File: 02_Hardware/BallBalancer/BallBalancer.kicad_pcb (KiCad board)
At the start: 2 copper layers, 43 parts, among them J1 ENCODER1_CON, J2 ENCODER2_CON, J3 USB_B_Micro, J4 SWD, Q1 DMN10H220L, U1 STM32L412K8Tx, U2 USBLC6-2SC6, U3 AP63203WU

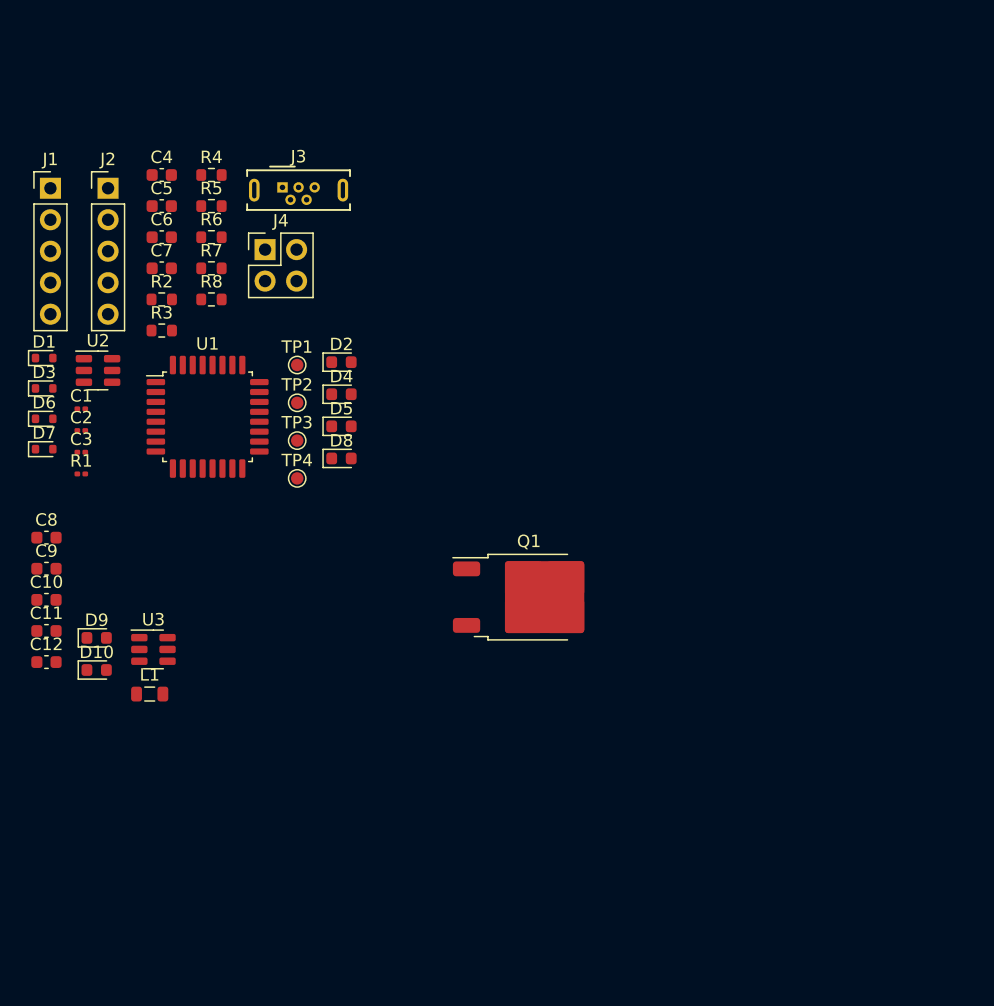
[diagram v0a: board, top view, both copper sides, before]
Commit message: Hardware schema and layout created
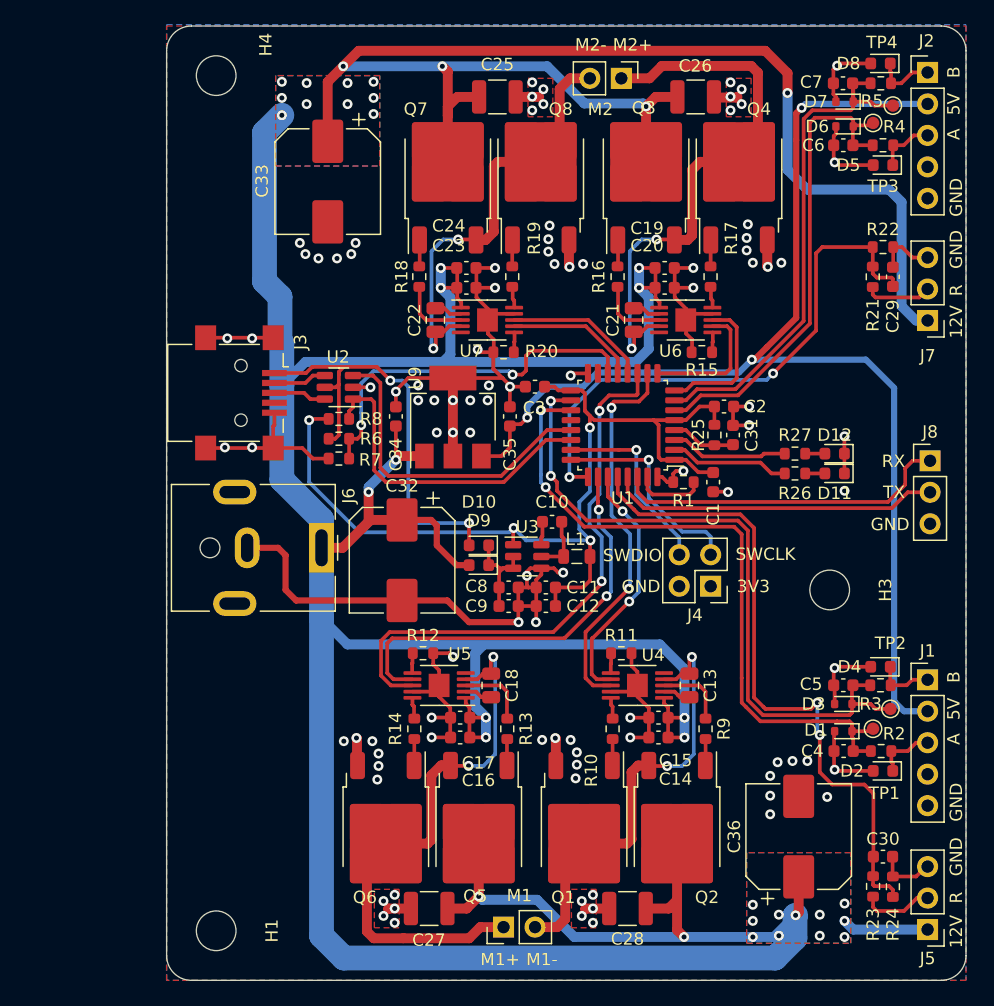
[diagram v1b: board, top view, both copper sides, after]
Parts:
- added C13: 1u, Capacitor_SMD:C_0805_2012Metric, F.Cu at (124.7, 111.2)
- added C14: 1u, Capacitor_SMD:C_0603_1608Metric, F.Cu at (122.2, 115.4)
- added C15: 100n, Capacitor_SMD:C_0603_1608Metric, F.Cu at (122.2, 113.8)
- added C16: 1u, Capacitor_SMD:C_0603_1608Metric, F.Cu at (106.2, 115.4)
- added C17: 100n, Capacitor_SMD:C_0603_1608Metric, F.Cu at (106.2, 113.8)
- added C18: 1u, Capacitor_SMD:C_0805_2012Metric, F.Cu at (108.7, 111.2)
- added C19: 1u, Capacitor_SMD:C_0603_1608Metric, F.Cu at (122.7, 77.5)
- added C20: 100n, Capacitor_SMD:C_0603_1608Metric, F.Cu at (122.7, 79.1)
- added C21: 1u, Capacitor_SMD:C_0805_2012Metric, F.Cu at (120.2, 81.7)
- added C22: 1u, Capacitor_SMD:C_0805_2012Metric, F.Cu at (104.2, 81.7)
- added C23: 100n, Capacitor_SMD:C_0603_1608Metric, F.Cu at (106.7, 79.1)
- added C24: 1u, Capacitor_SMD:C_0603_1608Metric, F.Cu at (106.7, 77.5)
- added C25: 10U, Capacitor_SMD:C_1210_3225Metric, F.Cu at (109.2, 63.7)
- added C26: 10U, Capacitor_SMD:C_1210_3225Metric, F.Cu at (125.2, 63.7)
- added C27: 10U, Capacitor_SMD:C_1210_3225Metric, F.Cu at (103.7, 129.2)
- added C28: 10U, Capacitor_SMD:C_1210_3225Metric, F.Cu at (119.7, 129.2)
- added C29: 100n, Capacitor_SMD:C_0603_1608Metric, F.Cu at (141.1, 78.2)
- added C30: 100n, Capacitor_SMD:C_0603_1608Metric, F.Cu at (140.3, 125.0)
- added C31: 100n, Capacitor_SMD:C_0603_1608Metric, F.Cu at (128.2, 91.0)
- added C32: 330u, Capacitor_SMD:CP_Elec_8x10, F.Cu at (101.5, 101.1)
- added C33: 330u, Capacitor_SMD:CP_Elec_8x10, F.Cu at (95.5, 70.5)
- added C34: 100n, Capacitor_SMD:C_0603_1608Metric, F.Cu at (101.0, 89.5)
- added C35: 100n, Capacitor_SMD:C_0603_1608Metric, F.Cu at (110.2, 89.5)
- added C36: 330u, Capacitor_SMD:CP_Elec_8x10, F.Cu at (133.5, 123.4)
- added D11: LED, LED_SMD:LED_0603_1608Metric, F.Cu at (136.4, 94.1)
- added D12: LED, LED_SMD:LED_0603_1608Metric, F.Cu at (136.4, 92.5)
- added H1: MountingHole, MountingHole:MountingHole_3.2mm_M3, F.Cu at (86.5, 131.0)
- added H3: MountingHole, MountingHole:MountingHole_3.2mm_M3, F.Cu at (136.0, 103.5)
- added H4: MountingHole, MountingHole:MountingHole_3.2mm_M3, F.Cu at (86.5, 62.0)
- added J5: Conn_01x03_Pin, Connector_PinHeader_2.54mm:PinHeader_1x03_P2.54mm_Vertical, F.Cu at (143.9, 130.9)
- added J6: Jack-DC, Connector_BarrelJack:BarrelJack_CUI_PJ-063AH_Horizontal, F.Cu at (95.0, 100.1)
- added J7: Conn_01x03_Pin, Connector_PinHeader_2.54mm:PinHeader_1x03_P2.54mm_Vertical, F.Cu at (143.9, 81.8)
- added J8: Conn_01x03_Pin, Connector_PinHeader_2.54mm:PinHeader_1x03_P2.54mm_Vertical, F.Cu at (144.1, 93.1)
- added M1: Motor_DC, Connector_PinHeader_2.54mm:PinHeader_1x02_P2.54mm_Vertical, F.Cu at (109.7, 130.7)
- added M2: Motor_DC, Connector_PinHeader_2.54mm:PinHeader_1x02_P2.54mm_Vertical, F.Cu at (119.2, 62.2)
- added Q2: DMN10H220L, Package_TO_SOT_SMD:TO-252-2, F.Cu at (123.7, 122.7)
- added Q3: DMN10H220L, Package_TO_SOT_SMD:TO-252-2, F.Cu at (121.2, 70.2)
- added Q4: DMN10H220L, Package_TO_SOT_SMD:TO-252-2, F.Cu at (128.7, 70.2)
- added Q5: DMN10H220L, Package_TO_SOT_SMD:TO-252-2, F.Cu at (107.7, 122.7)
- added Q6: DMN10H220L, Package_TO_SOT_SMD:TO-252-2, F.Cu at (100.2, 122.7)
- added Q7: DMN10H220L, Package_TO_SOT_SMD:TO-252-2, F.Cu at (105.2, 70.2)
- added Q8: DMN10H220L, Package_TO_SOT_SMD:TO-252-2, F.Cu at (112.7, 70.2)
- added R10: 20, Resistor_SMD:R_0603_1608Metric, F.Cu at (118.5, 114.7)
- added R11: 10k, Resistor_SMD:R_0603_1608Metric, F.Cu at (119.2, 108.6)
- added R12: 10k, Resistor_SMD:R_0603_1608Metric, F.Cu at (103.2, 108.6)
- added R13: 20, Resistor_SMD:R_0603_1608Metric, F.Cu at (110.0, 114.7)
- added R14: 20, Resistor_SMD:R_0603_1608Metric, F.Cu at (102.5, 114.7)
- added R15: 10k, Resistor_SMD:R_0603_1608Metric, F.Cu at (125.7, 84.3)
- added R16: 20, Resistor_SMD:R_0603_1608Metric, F.Cu at (118.9, 78.2)
- added R17: 20, Resistor_SMD:R_0603_1608Metric, F.Cu at (126.4, 78.2)
- added R18: 20, Resistor_SMD:R_0603_1608Metric, F.Cu at (102.9, 78.2)
- added R19: 20, Resistor_SMD:R_0603_1608Metric, F.Cu at (110.4, 78.2)
- added R20: 10k, Resistor_SMD:R_0603_1608Metric, F.Cu at (109.7, 84.3)
- added R21: 10k, Resistor_SMD:R_0603_1608Metric, F.Cu at (139.5, 78.2)
- added R22: 10k, Resistor_SMD:R_0603_1608Metric, F.Cu at (140.3, 75.8)
- added R23: 10k, Resistor_SMD:R_0603_1608Metric, F.Cu at (139.5, 127.4)
- added R24: 10k, Resistor_SMD:R_0603_1608Metric, F.Cu at (141.1, 127.4)
- added R25: 100K, Resistor_SMD:R_0603_1608Metric, F.Cu at (126.7, 91.0)
- added R26: 240, Resistor_SMD:R_0603_1608Metric, F.Cu at (133.2, 94.1)
- added R27: 240, Resistor_SMD:R_0603_1608Metric, F.Cu at (133.2, 92.5)
- added R9: 20, Resistor_SMD:R_0603_1608Metric, F.Cu at (126.0, 114.7)
- added U4: DGD0506A, Package_SO:MSOP-10-1EP_3x3mm_P0.5mm_EP1.68x1.88mm, F.Cu at (120.5, 111.2)
- added U5: DGD0506A, Package_SO:MSOP-10-1EP_3x3mm_P0.5mm_EP1.68x1.88mm, F.Cu at (104.5, 111.2)
- added U6: DGD0506A, Package_SO:MSOP-10-1EP_3x3mm_P0.5mm_EP1.68x1.88mm, F.Cu at (124.4, 81.7)
- added U7: DGD0506A, Package_SO:MSOP-10-1EP_3x3mm_P0.5mm_EP1.68x1.88mm, F.Cu at (108.4, 81.7)
- added U9: LM2937IMP5, Package_TO_SOT_SMD:SOT-223-3_TabPin2, F.Cu at (105.6, 89.5)
- C1, C2, C3: footprint Capacitor_SMD:C_0201_0603Metric -> Capacitor_SMD:C_0603_1608Metric
- J3: footprint Connector_USB:USB_Micro-B_Wuerth_614105150721_Vertical -> Connector_USB:USB_Mini-B_Lumberg_2486_01_Horizontal
- R1: footprint Resistor_SMD:R_0201_0603Metric -> Resistor_SMD:R_0603_1608Metric
- moved J1 81.1 mm to (143.9, 110.7)
- moved C4 72.0 mm to (137.1, 116.5), turned to 180 degrees
- moved D1 71.2 mm to (137.1, 114.9), turned to 180 degrees
- moved D7 70.4 mm to (137.2, 64.1), turned to 180 degrees
- moved D3 69.3 mm to (137.1, 112.7), turned to 180 degrees
- moved D6 68.8 mm to (137.2, 66.1), turned to 180 degrees
- moved R2 68.5 mm to (140.2, 116.5), turned to 180 degrees
- moved C5 67.2 mm to (137.1, 111.2), turned to 180 degrees
- moved J2 66.8 mm to (143.9, 61.7)
- moved R3 64.7 mm to (140.1, 111.2), turned to 180 degrees
- moved C7 57.0 mm to (137.1, 62.6), turned to 180 degrees
- moved TP4 56.7 mm to (141.1, 64.4)
- moved C6 55.5 mm to (137.1, 67.6), turned to 180 degrees
- moved TP1 55.0 mm to (139.5, 114.7)
- moved R5 54.9 mm to (140.1, 62.6), turned to 180 degrees
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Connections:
- net ENCODER1_A_OUT renamed /Main/ENCODER1_A_OUT
- net ENCODER1_B_OUT renamed /Main/ENCODER1_B_OUT
- net ENCODER2_A_OUT renamed /Main/ENCODER2_A_OUT
- net ENCODER2_B_OUT renamed /Main/ENCODER2_B_OUT
- C4 pad 1: ENCODER1_A -> /Main/ENCODER1_A
- C5 pad 1: ENCODER1_B -> /Main/ENCODER1_B
- C6 pad 1: ENCODER2_A -> /Main/ENCODER2_A
- C7 pad 1: ENCODER2_B -> /Main/ENCODER2_B
- D1 pad 1: ENCODER1_A -> /Main/ENCODER1_A
- D3 pad 1: ENCODER1_B -> /Main/ENCODER1_B
- D6 pad 1: ENCODER2_A -> /Main/ENCODER2_A
- D7 pad 1: ENCODER2_B -> /Main/ENCODER2_B
- J1 pad 4: ENCODER1_INDEX -> unconnected-(J1-Pin_4-Pad4)
- J2 pad 4: ENCODER2_INDEX -> unconnected-(J2-Pin_4-Pad4)
- J4 pad 3: SWCLK -> /Main/SWCLK
- J4 pad 4: SWDIO -> /Main/SWDIO
- Q1 pad 1: unconnected-(Q1-G-Pad1) -> Net-(Q1-G)
- Q1 pad 2: unconnected-(Q1-S-Pad2) -> Net-(M1--)
- Q1 pad 3: unconnected-(Q1-D-Pad3) -> GND
- R1 pad 1: Net-(U1-PB7) -> GND
- R1 pad 2: GND -> Net-(U1-PH3)
- R2 pad 2: ENCODER1_A -> /Main/ENCODER1_A
- R3 pad 2: ENCODER1_B -> /Main/ENCODER1_B
- R4 pad 2: ENCODER2_A -> /Main/ENCODER2_A
- R5 pad 2: ENCODER2_B -> /Main/ENCODER2_B
- R6 pad 2: VUSB -> /Main/VUSB
- R7 pad 2: VUSB -> /Main/VUSB
- R8 pad 1: USB_DP -> /Main/USB_DP
- TP1 pad 1: ENCODER1_A -> /Main/ENCODER1_A
- TP2 pad 1: ENCODER1_B -> /Main/ENCODER1_B
- TP3 pad 1: ENCODER2_A -> /Main/ENCODER2_A
- TP4 pad 1: ENCODER2_B -> /Main/ENCODER2_B
- U1 pad 10: unconnected-(U1-PA4-Pad10) -> IN_MOT_CH1L
- U1 pad 11: unconnected-(U1-PA5-Pad11) -> IN_MOT_CH1R
- U1 pad 12: unconnected-(U1-PA6-Pad12) -> IN_MOT_CH2L
- U1 pad 13: unconnected-(U1-PA7-Pad13) -> EN_MOT_CH2L
- U1 pad 14: unconnected-(U1-PB0-Pad14) -> /Main/VUSB
- U1 pad 18: unconnected-(U1-PA8-Pad18) -> /Main/ENCODER1_B
- U1 pad 19: unconnected-(U1-PA9-Pad19) -> /Main/ENCODER1_A
- U1 pad 2: unconnected-(U1-PC14-Pad2) -> /Main/LED1
- U1 pad 21: unconnected-(U1-PA11-Pad21) -> /Main/USB_DM
- U1 pad 22: unconnected-(U1-PA12-Pad22) -> /Main/USB_DP
- U1 pad 23: unconnected-(U1-PA13-Pad23) -> /Main/SWDIO
- U1 pad 24: unconnected-(U1-PA14-Pad24) -> /Main/SWCLK
- U1 pad 25: unconnected-(U1-PA15-Pad25) -> /Main/REF_MOT2
- U1 pad 26: unconnected-(U1-PB3-Pad26) -> EN_MOT_CH1R
- U1 pad 27: unconnected-(U1-PB4-Pad27) -> EN_MOT_CH1L
- U1 pad 28: unconnected-(U1-PB5-Pad28) -> /Main/REF_MOT1
- U1 pad 29: unconnected-(U1-PB6-Pad29) -> /Main/RSPI_TX
- U1 pad 3: unconnected-(U1-PC15-Pad3) -> /Main/LED2
- U1 pad 30: Net-(U1-PB7) -> /Main/RSPI_RX
- U1 pad 31: unconnected-(U1-PH3-Pad31) -> Net-(U1-PH3)
- U1 pad 4: unconnected-(U1-NRST-Pad4) -> Net-(U1-NRST)
- U1 pad 6: unconnected-(U1-PA0-Pad6) -> /Main/ENCODER2_A
- U1 pad 7: unconnected-(U1-PA1-Pad7) -> /Main/ENCODER2_B
- U1 pad 8: unconnected-(U1-PA2-Pad8) -> IN_MOT_CH2R
- U1 pad 9: unconnected-(U1-PA3-Pad9) -> EN_MOT_CH2R
- U2 pad 1: USB_DP -> /Main/USB_DP
- U2 pad 3: USB_DM -> /Main/USB_DM
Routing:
- net +12V: track 0.00 -> 424.7 mm, vias 0 -> 37
- net GND: track 0.00 -> 201.2 mm, vias 0 -> 99
- net +5V: track 0.00 -> 99.7 mm, vias 0 -> 3
- net +3V3: track 0.00 -> 77.7 mm, vias 0 -> 4
- net /Main/ENCODER1_B: track 0.00 -> 55.4 mm, vias 0 -> 2
- net /Main/ENCODER1_A: track 0.00 -> 54.9 mm, vias 0 -> 2
- net /Main/REF_MOT1: track 0.00 -> 53.3 mm, vias 0 -> 2
- net IN_MOT_CH1R: track 0.00 -> 45.7 mm, vias 0 -> 2
- net /Main/REF_MOT2: track 0.00 -> 45.0 mm, vias 0 -> 2
- net Net-(M2-+): track 0.00 -> 43.7 mm, vias 0 -> 2
- net Net-(M1-+): track 0.00 -> 43.5 mm, vias 0 -> 2
- net /Main/ENCODER2_B: track 0.00 -> 42.1 mm
- net /Main/ENCODER2_A: track 0.00 -> 39.2 mm
- net VBUS: track 0.00 -> 36.8 mm, vias 0 -> 2
- net EN_MOT_CH1R: track 0.00 -> 34.1 mm, vias 0 -> 2
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- added copper zone on B.Cu, net +12V
- added copper zone on F.Cu, net +12V
- added copper zone on B.Cu, net GND
- added copper zone on F.Cu, net GND
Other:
- board outline added: 64.5 x 77 mm
- board text added: "12V"
- board text added: "3V3"
- board text added: "5V"
- board text added: "A"
- board text added: "B"
- board text added: "GND"
- board text added: "M1+"
- board text added: "M1-"
- board text added: "M2+"
- board text added: "M2-"
- board text added: "R"
- board text added: "RX"
- board text added: "SWCLK"
- board text added: "SWDIO"
- board text added: "TX"

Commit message: ERC and DRC warnings and errors in schema and layout fixed
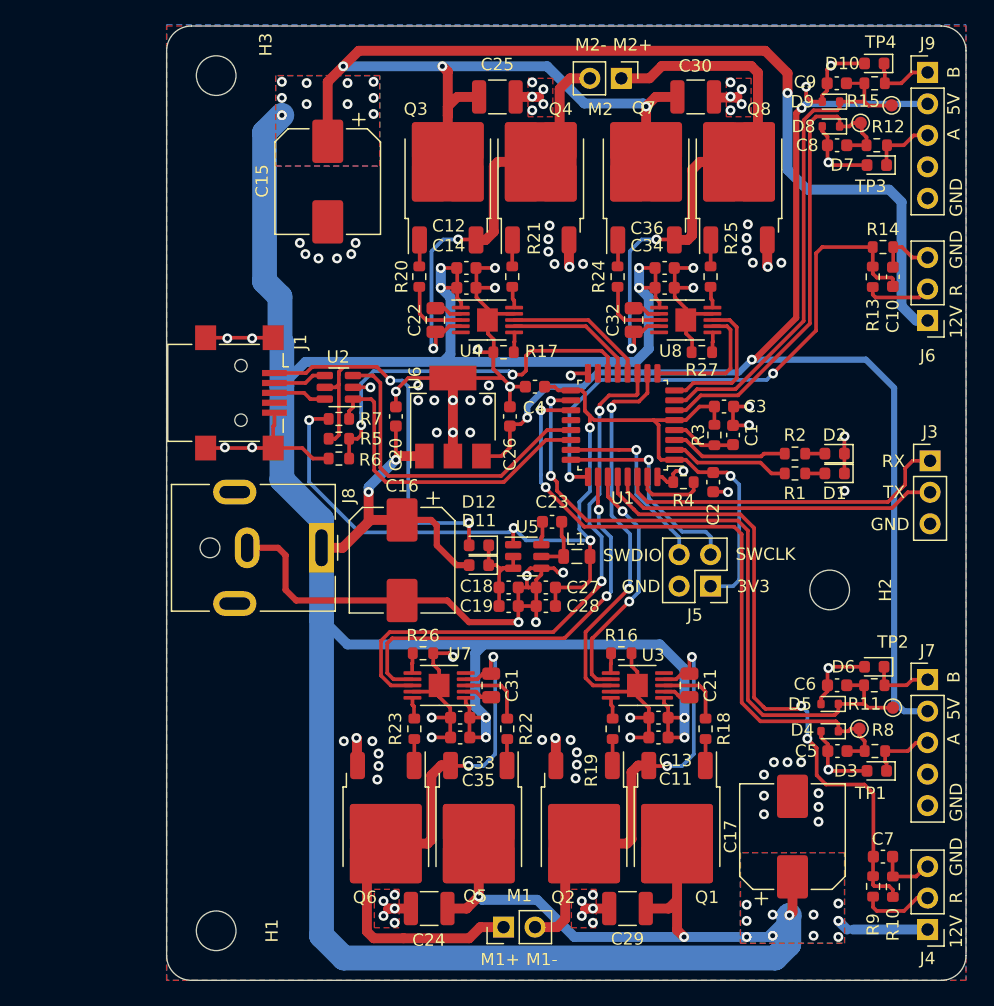
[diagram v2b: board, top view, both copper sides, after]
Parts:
- removed the J1 at (143.9, 110.7)
- removed J2: ENCODER2_CON, Connector_PinHeader_2.54mm:PinHeader_1x05_P2.54mm_Vertical
- removed the J4 at (126.4, 103.2)
- added J5: SWD, Connector_PinHeader_2.54mm:PinHeader_2x02_P2.54mm_Vertical, F.Cu at (126.4, 103.2)
- added J7: ENCODER 1, Connector_PinHeader_2.54mm:PinHeader_1x05_P2.54mm_Vertical, F.Cu at (143.9, 110.7)
- added J9: ENCODER 2, Connector_PinHeader_2.54mm:PinHeader_1x05_P2.54mm_Vertical, F.Cu at (143.9, 61.7)
- J3: renamed from J8; value Conn_01x03_Pin -> Raspberry PI UART
- J4: renamed from J5; value Conn_01x03_Pin -> Reference switch 1
- J6: renamed from J7; value Conn_01x03_Pin -> Reference switch 2
- R10: renamed from R24; value 10k -> 1K
- R13: renamed from R21; value 10k -> 2.7K
- R14: renamed from R22; value 10k -> 1K
- R9: renamed from R23; value 10k -> 2.7K
- moved D4 1.10 mm to (136.0, 114.9)
- moved D5 1.10 mm to (136.0, 112.7)
- moved D8 1.10 mm to (136.1, 66.1)
- moved D9 1.10 mm to (136.1, 64.1)
- moved TP1 1.10 mm to (138.4, 114.7)
- moved TP3 1.00 mm to (138.5, 65.8)
- moved C17 0.50 mm to (133.0, 123.4)
- moved C5 0.50 mm to (136.6, 116.5)
- moved C6 0.50 mm to (136.6, 111.2)
- moved C8 0.50 mm to (136.6, 67.6)
- moved C9 0.50 mm to (136.6, 62.6)
- moved D10 0.50 mm to (139.6, 61.0)
- moved D3 0.50 mm to (139.8, 118.1)
- moved D6 0.50 mm to (139.6, 109.7)
- moved D7 0.50 mm to (139.8, 69.2)
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- renumbered C31 to C1, C29 to C10, C14 to C11, C24 to C12, C15 to C13, C23 to C14, C33 to C15, C32 to C16, C36 to C17, C8 to C18, C9 to C19, C1 to C2, C34 to C20, C13 to C21, C10 to C23, C27 to C24, C35 to C26, C11 to C27, C12 to C28, C28 to C29, C2 to C3, C26 to C30, C18 to C31, C21 to C32, C17 to C33, C20 to C34, C16 to C35, C19 to C36, C3 to C4, C4 to C5, C5 to C6, C30 to C7, C6 to C8, C7 to C9, D11 to D1, D8 to D10, D9 to D11, D10 to D12, D12 to D2, D2 to D3, D1 to D4, D3 to D5, D4 to D6, D5 to D7, D6 to D8, D7 to D9, H3 to H2, H4 to H3, J3 to J1, J6 to J8, Q2 to Q1, Q1 to Q2, Q7 to Q3, Q8 to Q4, Q3 to Q7, Q4 to Q8, R26 to R1, R3 to R11, R4 to R12, R5 to R15, R11 to R16, R20 to R17, R9 to R18, R10 to R19, R27 to R2, R18 to R20, R19 to R21, R13 to R22, R14 to R23, R16 to R24, R17 to R25, R12 to R26, R15 to R27, R25 to R3, R1 to R4, R6 to R5, R7 to R6, R8 to R7, R2 to R8, U4 to U3, U7 to U4, U3 to U5, U9 to U6, U5 to U7, U6 to U8
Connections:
- net Net-(D10-K) renamed +12VA
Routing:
- net +3V3: track 77.7 -> 90.4 mm, vias 4 -> 5
- net GND: track 201.2 -> 203.8 mm, vias 99 -> 102
- net /Main/ENCODER2_B: track 42.1 -> 40.0 mm
- net /Main/REF_MOT1: track 53.3 -> 52.5 mm
- net /Main/ENCODER1_A: track 54.9 -> 54.1 mm
- net /Main/ENCODER2_B_OUT: track 4.94 -> 5.44 mm
- net /Main/ENCODER2_A_OUT: track 4.72 -> 5.22 mm
- net /Main/ENCODER1_B_OUT: track 4.66 -> 5.16 mm
- net /Main/ENCODER1_A_OUT: track 4.85 -> 5.35 mm

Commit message: Test points added and BOM created
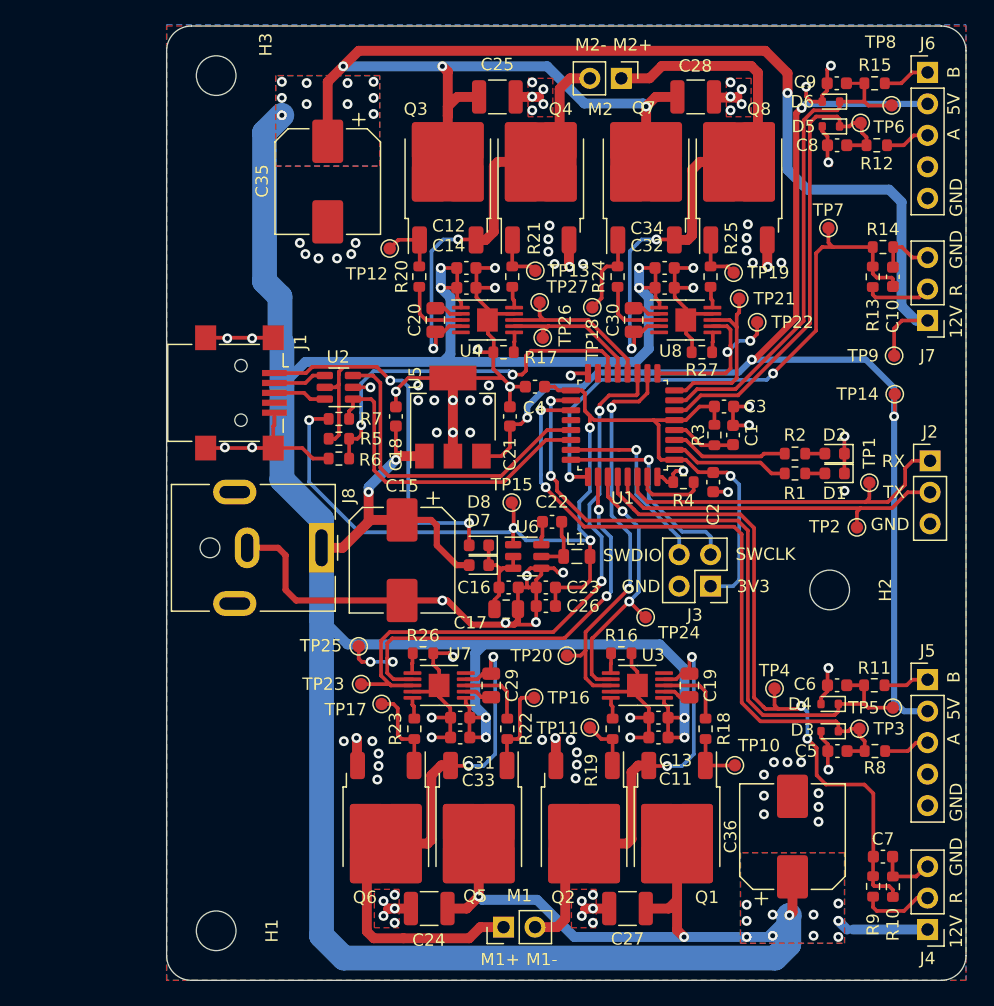
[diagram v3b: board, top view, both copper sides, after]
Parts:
- removed D10: D_TVS, Diode_SMD:D_0603_1608Metric
- removed the D3 at (139.8, 118.1)
- removed the D6 at (139.6, 109.7)
- removed the D7 at (139.8, 69.2)
- added TP1: UART_RX, TestPoint:TestPoint_Pad_D1.0mm, F.Cu at (139.2, 94.8)
- added TP10: GH_CH1L, TestPoint:TestPoint_Pad_D1.0mm, F.Cu at (128.3, 117.7)
- added TP11: GL_CH1L, TestPoint:TestPoint_Pad_D1.0mm, F.Cu at (116.7, 114.6)
- added TP12: GH_CH2L, TestPoint:TestPoint_Pad_D1.0mm, F.Cu at (100.5, 76.0)
- added TP13: GL_CH2L, TestPoint:TestPoint_Pad_D1.0mm, F.Cu at (112.2, 77.8)
- added TP14: 5V, TestPoint:TestPoint_Pad_D1.0mm, F.Cu at (141.2, 87.7)
- added TP15: 3.3V, TestPoint:TestPoint_Pad_D1.0mm, F.Cu at (110.3, 96.5)
- added TP16: GH_CH1R, TestPoint:TestPoint_Pad_D1.0mm, F.Cu at (112.2, 112.2)
- added TP17: GL_CH1R, TestPoint:TestPoint_Pad_D1.0mm, F.Cu at (99.8, 112.7)
- added TP18: GH_CH2R, TestPoint:TestPoint_Pad_D1.0mm, F.Cu at (116.8, 80.7)
- added TP19: GL_CH2R, TestPoint:TestPoint_Pad_D1.0mm, F.Cu at (128.2, 77.9)
- added TP2: UART_TX, TestPoint:TestPoint_Pad_D1.0mm, F.Cu at (138.2, 98.5)
- added TP20: IN_CH2R, TestPoint:TestPoint_Pad_D1.0mm, F.Cu at (114.8, 108.8)
- added TP21: IN_CH2R, TestPoint:TestPoint_Pad_D1.0mm, F.Cu at (128.7, 80.0)
- added TP22: IN_CH2R, TestPoint:TestPoint_Pad_D1.0mm, F.Cu at (130.2, 81.9)
- added TP23: IN_CH2R, TestPoint:TestPoint_Pad_D1.0mm, F.Cu at (98.2, 111.1)
- added TP24: IN_CH2R, TestPoint:TestPoint_Pad_D1.0mm, F.Cu at (121.2, 105.7)
- added TP25: IN_CH2R, TestPoint:TestPoint_Pad_D1.0mm, F.Cu at (98.0, 108.0)
- added TP26: IN_CH2R, TestPoint:TestPoint_Pad_D1.0mm, F.Cu at (112.8, 83.2)
- added TP27: IN_CH2R, TestPoint:TestPoint_Pad_D1.0mm, F.Cu at (112.6, 80.3)
- added TP4: REF_MOT1, TestPoint:TestPoint_Pad_D1.0mm, F.Cu at (131.6, 111.5)
- added TP7: REF_MOT2, TestPoint:TestPoint_Pad_D1.0mm, F.Cu at (135.9, 74.3)
- added TP9: 12V, TestPoint:TestPoint_Pad_D1.0mm, F.Cu at (141.2, 84.6)
- C17: renamed from C19; footprint Capacitor_SMD:C_0603_1608Metric -> Capacitor_SMD:C_0805_2012Metric
- C19: renamed from C21; value 1u -> 1000p
- C2, C3, C4: value C -> 100n
- C20: renamed from C22; value 1u -> 1000p
- C24, C25: value 10U -> 10u
- C27: renamed from C29; value 10U -> 10u
- C28: renamed from C30; value 10U -> 10u
- C29: renamed from C31; value 1u -> 1000p
- C30: renamed from C32; value 1u -> 1000p
- D1: value LED -> LED_R
- D2: value LED -> LED_G
- R10, R14: value 1K -> 1k
- R13, R9: value 2.7K -> 3.3k
- R18, R19, R20, R21, R22, R23, R24, R25: value 20 -> 120
- R3: value 100K -> 100k
- moved C17 0.32 mm to (109.9, 105.0)
- renumbered C16 to C15, C18 to C16, C20 to C18, C26 to C21, C23 to C22, C27 to C23, C28 to C26, C33 to C31, C34 to C32, C35 to C33, C36 to C34, C15 to C35, C17 to C36, D4 to D3, D5 to D4, D8 to D5, D9 to D6, D11 to D7, D12 to D8, J3 to J2, J5 to J3, J7 to J5, J9 to J6, J6 to J7, TP1 to TP3, TP2 to TP5, TP3 to TP6, TP4 to TP8, U6 to U5, U5 to U6
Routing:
- net GND: track 203.8 -> 193.2 mm, vias 102 -> 103
- net Net-(Q5-G): track 2.14 -> 7.44 mm
- net +12V: track 424.5 -> 429.7 mm
- net Net-(Q6-G): track 2.14 -> 7.21 mm
- net Net-(Q7-G): track 2.11 -> 6.78 mm
- net EN_MOT_CH2R: track 10.8 -> 15.4 mm, vias 0 -> 2
- net EN_MOT_CH1R: track 34.1 -> 38.5 mm, vias 2 -> 4
- net Net-(Q3-G): track 2.11 -> 4.82 mm
- net IN_MOT_CH1R: track 45.7 -> 48.1 mm
- net Net-(Q1-G): track 2.14 -> 4.53 mm
- net IN_MOT_CH2R: track 11.7 -> 14.1 mm
- net Net-(Q2-G): track 2.14 -> 4.37 mm
- net +3V3: track 90.4 -> 92.5 mm
- net Net-(Q8-G): track 2.14 -> 4.21 mm
- net Net-(Q4-G): track 2.14 -> 4.15 mm
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
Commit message: CAD files and hardware manufacturing data added
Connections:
- U1 pad 10: IN_MOT_CH1L -> EN_MOT_CH2R
- U1 pad 11: IN_MOT_CH1R -> unconnected-(U1-PA5-Pad11)
- U1 pad 20: unconnected-(U1-PA10-Pad20) -> IN_MOT_CH1R
- U1 pad 9: EN_MOT_CH2R -> IN_MOT_CH1L
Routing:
- net IN_MOT_CH1R: track 48.1 -> 43.7 mm
- net EN_MOT_CH2R: track 15.4 -> 18.7 mm
- net +3V3: track 92.5 -> 93.7 mm
